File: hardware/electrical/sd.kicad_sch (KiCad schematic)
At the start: 0 parts

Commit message: Add SD card to schematic
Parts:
- added C35: 4u7, symbol Device:C
- added C36: 100n, symbol Device:C
- added J4: Micro_SD_Card_Det, symbol Connector:Micro_SD_Card_Det
- added R20, R21, R22, R23, R24, R25: 10k, symbol Device:R
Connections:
- new net +3V3: C35.1, C36.1, J4.4 (VDD), R20.1, R21.1, R22.1, R23.1, R24.1, R25.1
- new net GND: C35.2, C36.2, J4.11 (SHIELD), J4.6 (VSS), J4.9 (DET_B)
- new net SDIO_CK: J4.5 (CLK)
- new net SDIO_CMD: J4.3 (CMD), R22.2
- new net SDIO_D0: J4.7 (DAT0), R23.2
- new net SDIO_D1: J4.8 (DAT1), R24.2
- new net SDIO_D2: J4.1 (DAT2), R20.2
- new net SDIO_D3: J4.2 (DAT3/CD), R21.2
- new net SD_DETECT: J4.10 (DET_A), R25.2
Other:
- company: (none) -> Frank Plowman
- title: (none) -> SD

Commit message: Fix schematic formatting (#6)
* Fix schematic formatting

* Clear and re-annotate to fix ERC
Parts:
- renumbered J4 to J3, R20 to R13, R21 to R14, R22 to R15, R23 to R16, R24 to R17, R25 to R18
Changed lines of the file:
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@@
   (symbol (lib_id "power:+3V3") (at 140.97 88.9 0) (unit 1)
     (in_bom yes) (on_board yes)
-    (property "Reference" "#PWR066" (id 0) (at 140.97 92.71 0)
+    (property "Reference" "#PWR060" (id 0) (at 140.97 92.71 0)
       (effects (font (size 1.27 1.27)) hide)
     )
@@
   (symbol (lib_id "power:GND") (at 147.32 67.31 0) (unit 1)
     (in_bom yes) (on_board yes) (fields_autoplaced)
-    (property "Reference" "#PWR067" (id 0) (at 147.32 73.66 0)
+    (property "Reference" "#PWR061" (id 0) (at 147.32 73.66 0)
       (effects (font (size 1.27 1.27)) hide)
     )
@@
   (symbol (lib_id "Device:R") (at 105.41 92.71 0) (unit 1)
     (in_bom yes) (on_board yes) (fields_autoplaced)
-    (property "Reference" "R20" (id 0) (at 107.95 91.4399 0)
+    (property "Reference" "R13" (id 0) (at 107.95 91.4399 0)
       (effects (font (size 1.27 1.27)) (justify left))
     )
@@
   (symbol (lib_id "Device:R") (at 123.19 92.71 0) (unit 1)
     (in_bom yes) (on_board yes) (fields_autoplaced)
-    (property "Reference" "R22" (id 0) (at 125.73 91.4399 0)
+    (property "Reference" "R15" (id 0) (at 125.73 91.4399 0)
       (effects (font (size 1.27 1.27)) (justify left))
     )
@@
   (symbol (lib_id "Device:R") (at 132.08 92.71 0) (unit 1)
     (in_bom yes) (on_board yes) (fields_autoplaced)
-    (property "Reference" "R23" (id 0) (at 134.62 91.4399 0)
+    (property "Reference" "R16" (id 0) (at 134.62 91.4399 0)
       (effects (font (size 1.27 1.27)) (justify left))
     )
@@
   (symbol (lib_id "power:+3V3") (at 132.08 88.9 0) (unit 1)
     (in_bom yes) (on_board yes)
-    (property "Reference" "#PWR064" (id 0) (at 132.08 92.71 0)
+    (property "Reference" "#PWR058" (id 0) (at 132.08 92.71 0)
       (effects (font (size 1.27 1.27)) hide)
     )
@@
   (symbol (lib_id "power:+3V3") (at 157.48 53.34 0) (unit 1)
     (in_bom yes) (on_board yes) (fields_autoplaced)
-    (property "Reference" "#PWR069" (id 0) (at 157.48 57.15 0)
+    (property "Reference" "#PWR063" (id 0) (at 157.48 57.15 0)
       (effects (font (size 1.27 1.27)) hide)
     )
@@
   (symbol (lib_id "power:GND") (at 157.48 129.54 0) (unit 1)
     (in_bom yes) (on_board yes) (fields_autoplaced)
-    (property "Reference" "#PWR070" (id 0) (at 157.48 135.89 0)
+    (property "Reference" "#PWR064" (id 0) (at 157.48 135.89 0)
       (effects (font (size 1.27 1.27)) hide)
     )
@@
   (symbol (lib_id "Device:R") (at 114.3 92.71 0) (unit 1)
     (in_bom yes) (on_board yes) (fields_autoplaced)
-    (property "Reference" "R21" (id 0) (at 116.84 91.4399 0)
+    (property "Reference" "R14" (id 0) (at 116.84 91.4399 0)
       (effects (font (size 1.27 1.27)) (justify left))
     )
@@
   (symbol (lib_id "power:+3V3") (at 105.41 88.9 0) (unit 1)
     (in_bom yes) (on_board yes) (fields_autoplaced)
-    (property "Reference" "#PWR061" (id 0) (at 105.41 92.71 0)
+    (property "Reference" "#PWR055" (id 0) (at 105.41 92.71 0)
       (effects (font (size 1.27 1.27)) hide)
     )
@@
   (symbol (lib_id "power:GND") (at 205.74 129.54 0) (unit 1)
     (in_bom yes) (on_board yes) (fields_autoplaced)
-    (property "Reference" "#PWR071" (id 0) (at 205.74 135.89 0)
+    (property "Reference" "#PWR065" (id 0) (at 205.74 135.89 0)
       (effects (font (size 1.27 1.27)) hide)
     )
@@
   (symbol (lib_id "Connector:Micro_SD_Card_Det") (at 182.88 109.22 0) (unit 1)
     (in_bom yes) (on_board yes) (fields_autoplaced)
-    (property "Reference" "J4" (id 0) (at 183.515 90.17 0))
+    (property "Reference" "J3" (id 0) (at 183.515 90.17 0))
     (property "Value" "Micro_SD_Card_Det" (id 1) (at 183.515 90.17 0)
       (effects (font (size 1.27 1.27)) hide)
@@
   (symbol (lib_id "Device:R") (at 149.86 92.71 0) (unit 1)
     (in_bom yes) (on_board yes) (fields_autoplaced)
-    (property "Reference" "R25" (id 0) (at 152.4 91.4399 0)
+    (property "Reference" "R18" (id 0) (at 152.4 91.4399 0)
       (effects (font (size 1.27 1.27)) (justify left))
     )
@@
   (symbol (lib_id "power:+3V3") (at 114.3 88.9 0) (unit 1)
     (in_bom yes) (on_board yes) (fields_autoplaced)
-    (property "Reference" "#PWR062" (id 0) (at 114.3 92.71 0)
+    (property "Reference" "#PWR056" (id 0) (at 114.3 92.71 0)
       (effects (font (size 1.27 1.27)) hide)
     )
@@
   (symbol (lib_id "Device:R") (at 140.97 92.71 0) (unit 1)
     (in_bom yes) (on_board yes) (fields_autoplaced)
-    (property "Reference" "R24" (id 0) (at 143.51 91.4399 0)
+    (property "Reference" "R17" (id 0) (at 143.51 91.4399 0)
       (effects (font (size 1.27 1.27)) (justify left))
     )
@@
   (symbol (lib_id "power:GND") (at 134.62 67.31 0) (unit 1)
     (in_bom yes) (on_board yes) (fields_autoplaced)
-    (property "Reference" "#PWR065" (id 0) (at 134.62 73.66 0)
+    (property "Reference" "#PWR059" (id 0) (at 134.62 73.66 0)
       (effects (font (size 1.27 1.27)) hide)
     )
@@
   (symbol (lib_id "power:+3V3") (at 149.86 88.9 0) (unit 1)
     (in_bom yes) (on_board yes)
-    (property "Reference" "#PWR068" (id 0) (at 149.86 92.71 0)
+    (property "Reference" "#PWR062" (id 0) (at 149.86 92.71 0)
       (effects (font (size 1.27 1.27)) hide)
     )
@@
   (symbol (lib_id "power:+3V3") (at 123.19 88.9 0) (unit 1)
     (in_bom yes) (on_board yes) (fields_autoplaced)
-    (property "Reference" "#PWR063" (id 0) (at 123.19 92.71 0)
-      (effects (font (size 1.27 1.27)) hide)
-    )
+    (property "Reference" "#PWR057" (id 0) (at 123.19 92.71 0)
+      (effects (font (size 1.27 1.27)) hide)
+    )

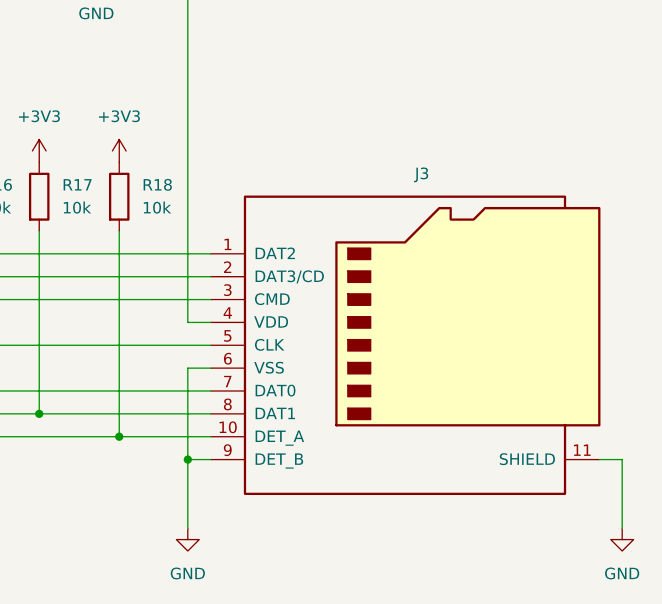
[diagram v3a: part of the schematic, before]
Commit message: Update footprints to KiCad 7.0 versions
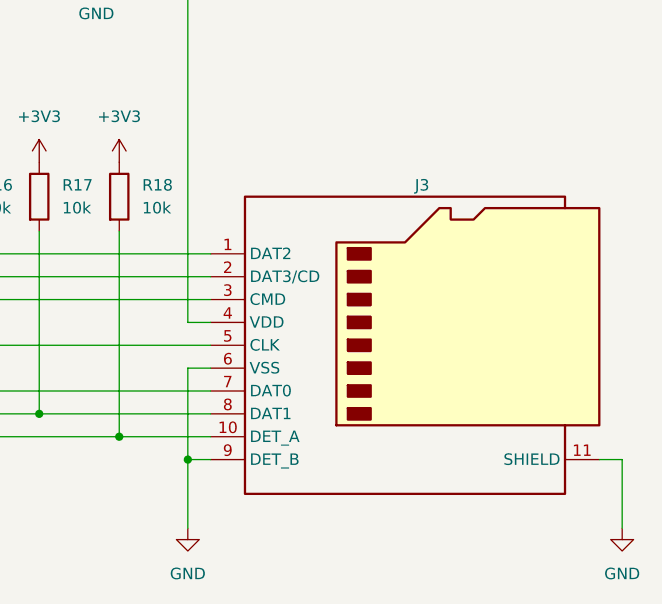
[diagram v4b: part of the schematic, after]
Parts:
- removed J3: Micro_SD_Card_Det, symbol Connector:Micro_SD_Card_Det
- added J3: Micro_SD_Card_Det2, symbol Connector:Micro_SD_Card_Det2
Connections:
- net +3V3: now also J3.4 (VDD)
- net GND: now also J3.11 (SHIELD), J3.6 (VSS), J3.9 (DET_B)
- net SDIO_CK: now also J3.5 (CLK)
- net SDIO_CMD: now also J3.3 (CMD)
- net SDIO_D0: now also J3.7 (DAT0)
- net SDIO_D1: now also J3.8 (DAT1)
- net SDIO_D2: now also J3.1 (DAT2)
- net SDIO_D3: now also J3.2 (DAT3/CD)
- net SD_DETECT: now also J3.10 (DET_A)
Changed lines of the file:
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@@
+    )
+  )
+  (symbol (lib_id "Connector:Micro_SD_Card_Det2") (at 182.88 109.22 0) (unit 1)
+    (in_bom yes) (on_board yes) (dnp no) (fields_autoplaced)
+    (property "Reference" "J3" (at 183.515 91.44 0)
+      (effects (font (size 1.27 1.27)))
+    )
+    (property "Value" "Micro_SD_Card_Det2" (at 183.515 91.44 0)
+      (effects (font (size 1.27 1.27)) hide)
+    )
+    (property "Footprint" "" (at 234.95 91.44 0)
+      (effects (font (size 1.27 1.27)) hide)
+    )
+    (property "Datasheet" "https://www.hirose.com/en/product/document?clcode=&productname=&series=DM3&documenttype=Catalog&lang=en&documentid=D49662_en" (at 185.42 106.68 0)
+      (effects (font (size 1.27 1.27)) hide)
+    )
+    (pin "1")
+    (pin "10")
+    (pin "11")
+    (pin "2")
+    (pin "3")
+    (pin "4")
+    (pin "5")
+    (pin "6")
+    (pin "7")
+    (pin "8")
+    (pin "9")
+    (instances
+      (project "3885"
+        (path "/7363a4f0-2da1-4086-abed-ea6709c3a185/6cde842e-a6be-40ad-bea6-4575bf07edd2"
+          (reference "J3") (unit 1)
+        )
+      )
     )
   )
@@
         )
       )
-    )
-  )
-  (symbol (lib_id "Connector:Micro_SD_Card_Det") (at 182.88 109.22 0) (unit 1)
-    (in_bom yes) (on_board yes) (dnp no) (fields_autoplaced)
-    (property "Reference" "J3" (at 183.515 90.17 0)
-      (effects (font (size 1.27 1.27)))
-    )
-    (property "Value" "Micro_SD_Card_Det" (at 183.515 90.17 0)
-      (effects (font (size 1.27 1.27)) hide)
-    )
-    (property "Footprint" "" (at 234.95 91.44 0)
-      (effects (font (size 1.27 1.27)) hide)
-    )
-    (property "Datasheet" "https://www.hirose.com/product/en/download_file/key_name/DM3/category/Catalog/doc_file_id/49662/?file_category_id=4&item_id=195&is_series=1" (at 182.88 106.68 0)
-      (effects (font (size 1.27 1.27)) hide)
-    )
-    (pin "1")
-    (pin "10")
-    (pin "11")
-    (pin "2")
-    (pin "3")
-    (pin "4")
-    (pin "5")
-    (pin "6")
-    (pin "7")
-    (pin "8")
-    (pin "9")
-    (instances
-      (project "3885"
-        (path "/7363a4f0-2da1-4086-abed-ea6709c3a185/6cde842e-a6be-40ad-bea6-4575bf07edd2"
-          (reference "J3") (unit 1)
-        )
-      )
